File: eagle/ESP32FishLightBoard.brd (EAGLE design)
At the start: 73.6 x 27.6 mm, 5 parts, among them J1 1X2-3.5MM, U1 SN74HCT04N

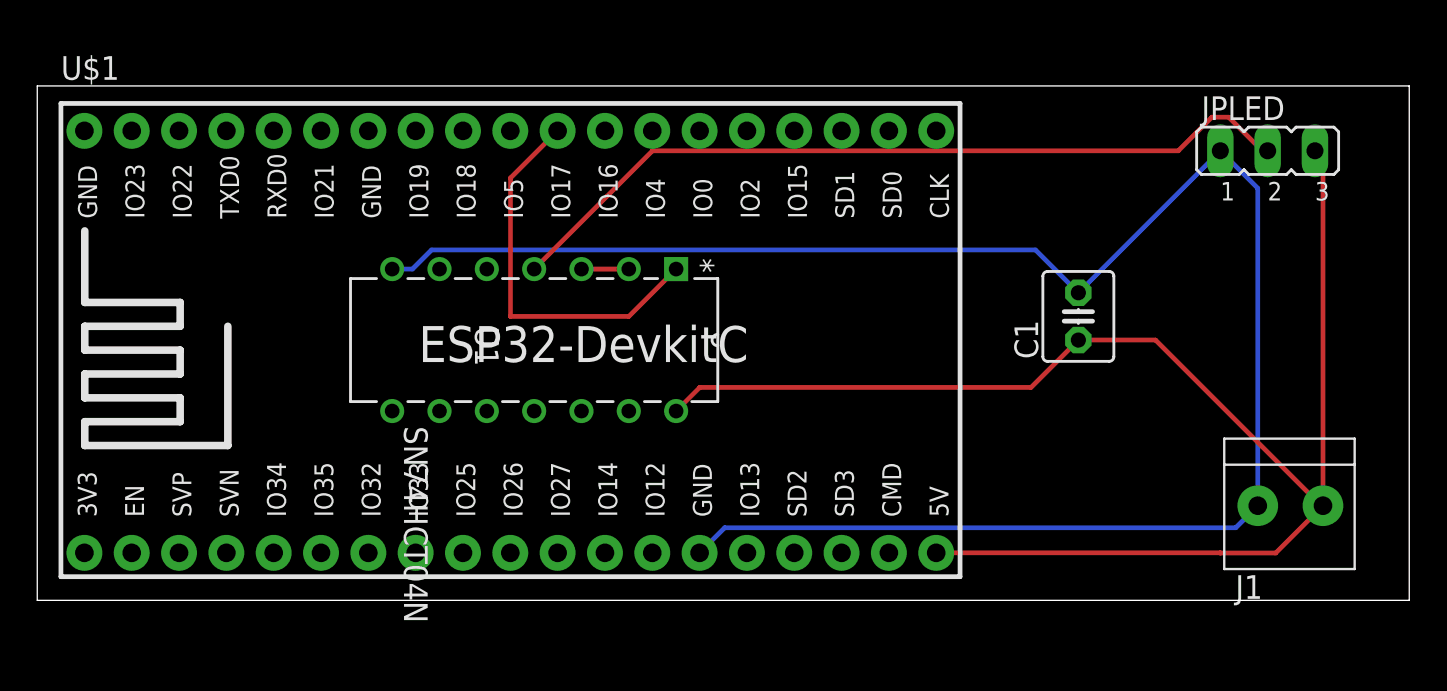
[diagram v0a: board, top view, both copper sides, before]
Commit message: added pull-down resistor to board
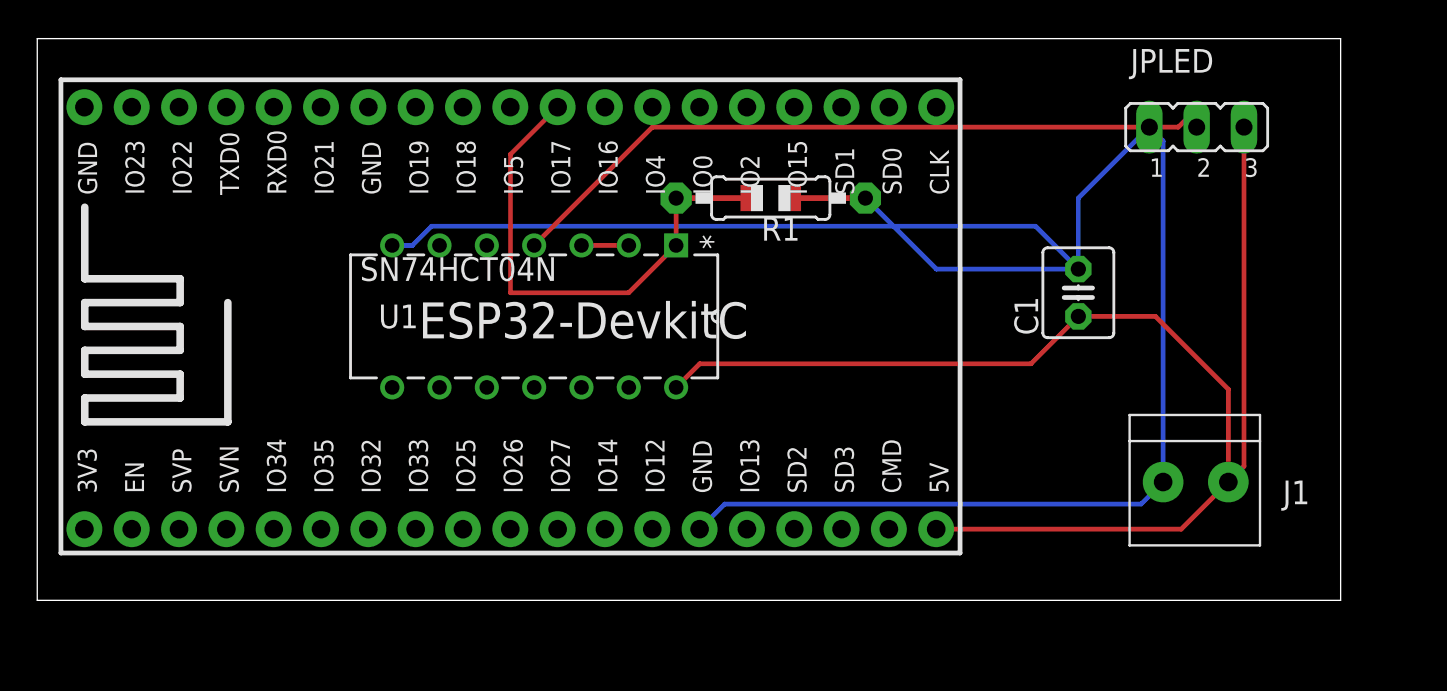
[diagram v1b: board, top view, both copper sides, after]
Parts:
- added R1: 4.7k, adafruit:0805-THM
- moved J1 5.24 mm to (62.2, 6.35)
- moved JPLED 4.02 mm to (62.2, 25.4)
- moved C1 1.27 mm to (55.9, 16.5)
- moved U$1 1.27 mm to (25.4, 15.2)
- moved U1 1.27 mm to (19.1, 11.4)
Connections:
- net GND: now also R1.2
- net IO17: now also R1.1
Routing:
- net VCC: track 81.4 -> 74.1 mm
- net GND: track 100.0 -> 105.9 mm
- net IO17_5V: track 43.5 -> 39.6 mm
- net IO17: track 21.0 -> 23.5 mm
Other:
- board size 73.6 x 27.6 mm -> 70 x 30.1 mm
